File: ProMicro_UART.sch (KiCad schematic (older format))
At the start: 54 parts, among them J2 Conn_01x06, J3 USB_B_Mini, U1 FT232H, U2 93CxxB, U3 AZ1117-3.3, Y1 12Mhz

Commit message: renamed files
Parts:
- removed JP10, JP11: Jumper_NO_Small, Jumper:SolderJumper-2_P1.3mm_Open_RoundedPad1.0x1.5mm, symbol Device:Jumper_NO_Small
- added JP10, JP11: Jumper_3_Bridged12, Jumper:SolderJumper-3_P1.3mm_Open_RoundedPad1.0x1.5mm, symbol Jumper:Jumper_3_Bridged12
- added U4: FT232RL, Package_DFN_QFN:QFN-32-1EP_5x5mm_P0.5mm_EP3.1x3.1mm, symbol Interface_USB:FT232RL
- C14: value 100n -> 1µ
- LOGO1: footprint Symbol:OSHW-Logo_5.7x6mm_SilkScreen -> Symbol:OSHW-Symbol_6.7x6mm_SilkScreen
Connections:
- net ADBUS0: now also JP10.3 (B), JP11.1 (A)
- net ADBUS1: now also JP10.1 (A), JP11.3 (B)
- net D0: now also JP11.2 (C)
- net D1: now also JP10.2 (C)
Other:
- note added: "ATTENTION:\nRXD & TXD are swapped here!"
- note added: "RXD & TXD\ncan swapped here"
- note added: "VBAT/2"
- note removed: "VBAT"
- moved on the sheet: C13, C14, JP12, JP13, JP14, JP15, U3

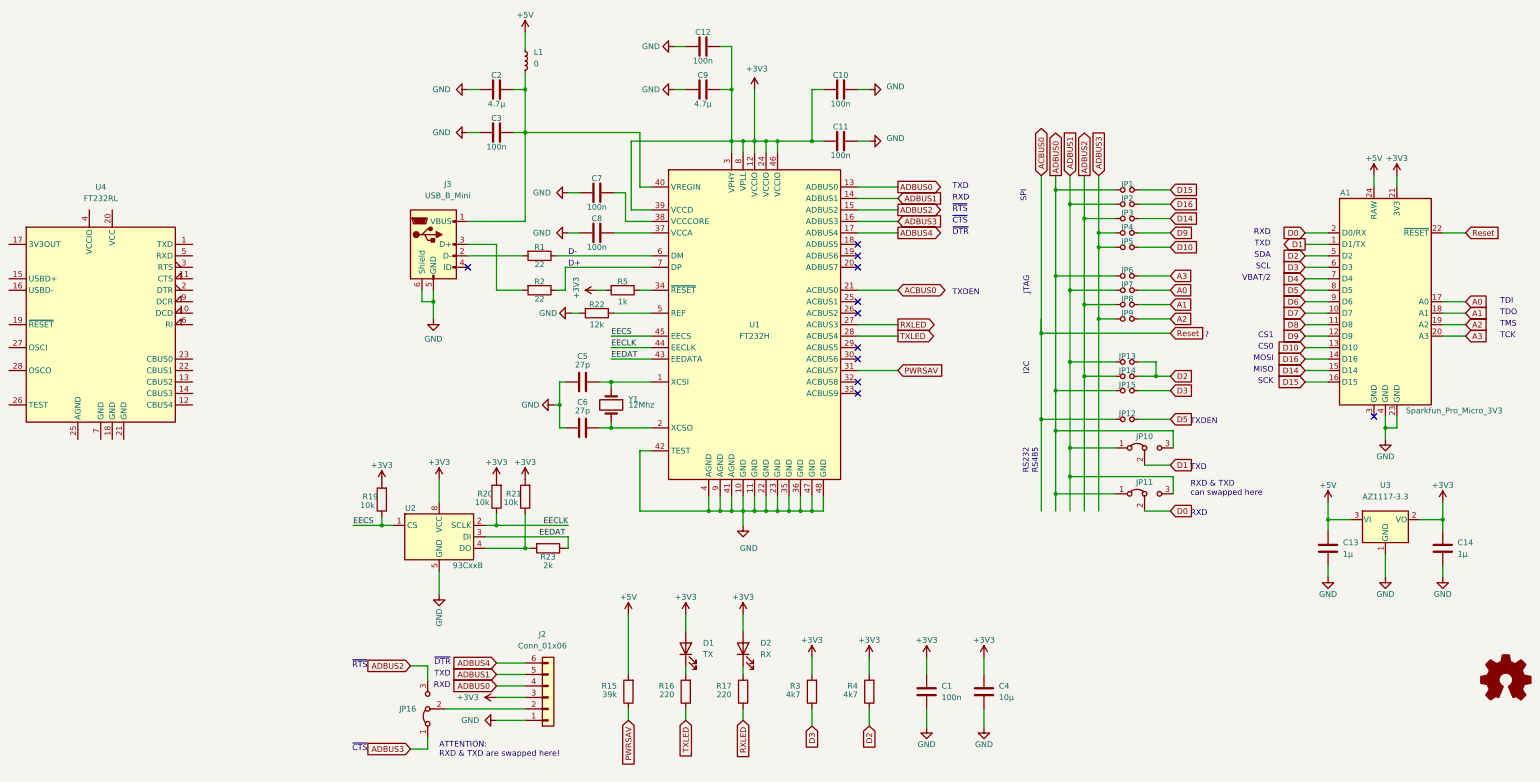
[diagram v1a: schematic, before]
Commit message: fully routed
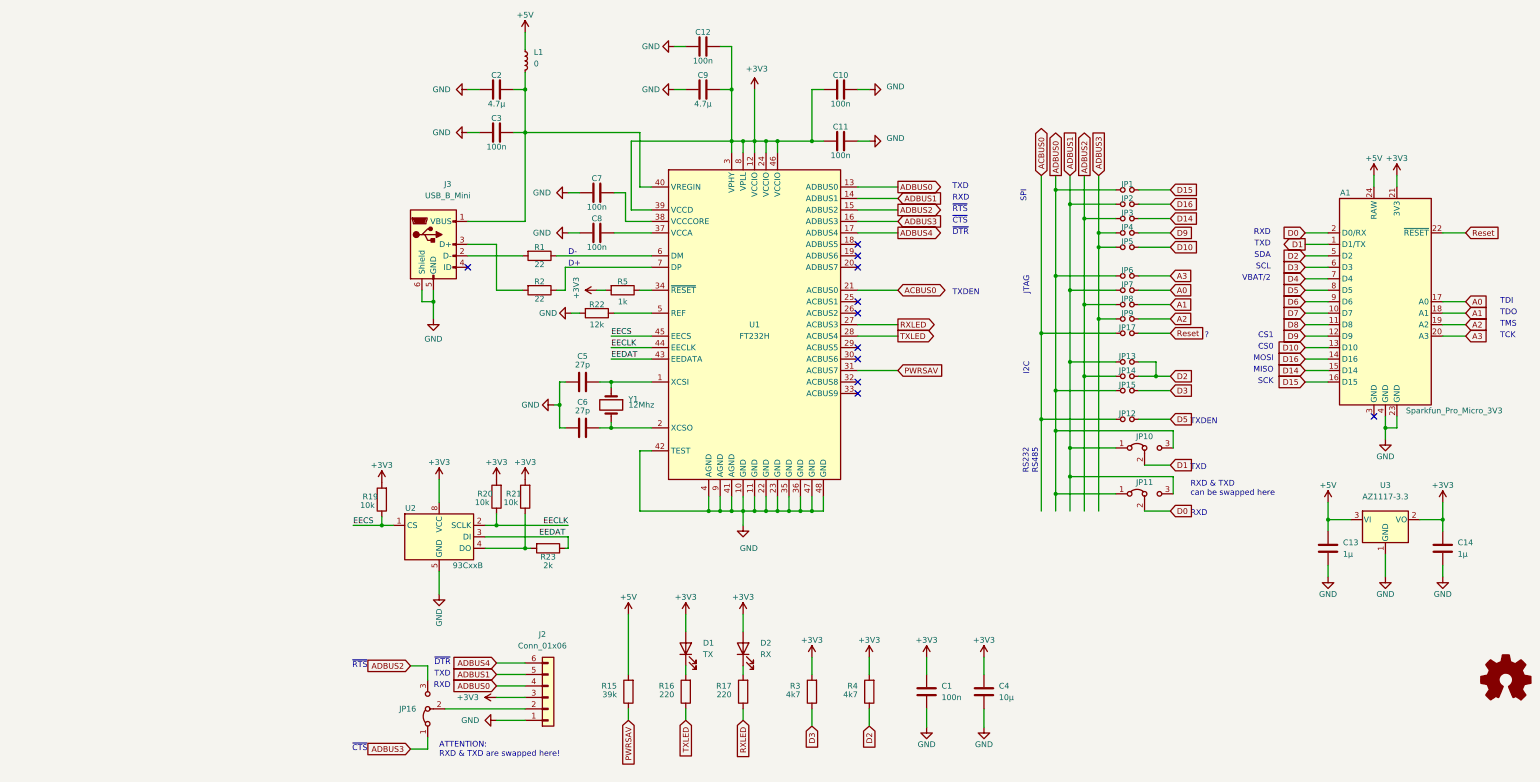
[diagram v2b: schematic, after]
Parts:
- removed U4: FT232RL, Package_DFN_QFN:QFN-32-1EP_5x5mm_P0.5mm_EP3.1x3.1mm, symbol Interface_USB:FT232RL
- added JP17: Jumper_NO_Small, Jumper:SolderJumper-2_P1.3mm_Open_RoundedPad1.0x1.5mm, symbol Device:Jumper_NO_Small
- U1: footprint Package_DFN_QFN:QFN-48-1EP_8x8mm_P0.5mm_EP6.2x6.2mm -> Package_QFP:LQFP-48_7x7mm_P0.5mm
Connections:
- net ACBUS0: now also JP17.1; no longer A1.22 (~RESET)
- new net Reset: A1.22 (~RESET), JP17.2
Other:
- note added: "RXD & TXD\ncan be swapped here"
- note removed: "RXD & TXD\ncan swapped here"

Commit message: new docs
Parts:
- added JP?: Jumper_NO_Small, symbol Device:Jumper_NO_Small
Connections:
- net +3V3: now also JP?.2
- net +5V: now also JP?.1
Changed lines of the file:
@@
 U 1 1 5EE683B5
 P 9750 5500
-F 0 "U3" H 9750 5800 50  0000 C CNN
-F 1 "AZ1117-3.3" H 9750 5700 50  0000 C CNN
+F 0 "U3" H 9750 5700 50  0000 C CNN
+F 1 "AZ1117-3.3" H 9750 5625 50  0000 C CNN
 F 2 "Package_TO_SOT_SMD:SOT-23-5" H 9750 5750 50  0001 C CIN
 F 3 "https://www.diodes.com/assets/Datasheets/AZ1117.pdf" H 9750 5500 50  0001 C CNN
@@
 L power:+5V #PWR0135
 U 1 1 5EE78093
-P 9250 5350
-F 0 "#PWR0135" H 9250 5200 50  0001 C CNN
-F 1 "+5V" H 9250 5500 50  0000 C CNN
-F 2 "" H 9250 5350 50  0001 C CNN
-F 3 "" H 9250 5350 50  0001 C CNN
-	1    9250 5350
+P 9250 5150
+F 0 "#PWR0135" H 9250 5000 50  0001 C CNN
+F 1 "+5V" H 9250 5300 50  0000 C CNN
+F 2 "" H 9250 5150 50  0001 C CNN
+F 3 "" H 9250 5150 50  0001 C CNN
+	1    9250 5150
 	1    0    0    -1
 $EndComp
@@
 L power:+3V3 #PWR0136
 U 1 1 5EE7895F
-P 10250 5350
-F 0 "#PWR0136" H 10250 5200 50  0001 C CNN
-F 1 "+3V3" H 10250 5500 50  0000 C CNN
-F 2 "" H 10250 5350 50  0001 C CNN
-F 3 "" H 10250 5350 50  0001 C CNN
-	1    10250 5350
+P 10250 5150
+F 0 "#PWR0136" H 10250 5000 50  0001 C CNN
+F 1 "+3V3" H 10250 5300 50  0000 C CNN
+F 2 "" H 10250 5150 50  0001 C CNN
+F 3 "" H 10250 5150 50  0001 C CNN
+	1    10250 5150
 	1    0    0    -1
 $EndComp
@@
 Connection ~ 9250 5500
 Wire Wire Line
-	9250 5500 9250 5350
+	9250 5500 9250 5175
 Wire Wire Line
 	10050 5500 10250 5500
 Wire Wire Line
-	10250 5500 10250 5350
+	10250 5500 10250 5175
 Wire Wire Line
 	10250 5600 10250 5500
@@
 Wire Wire Line
 	6750 3875 6750 4625
+$Comp
+L Device:Jumper_NO_Small JP?
+U 1 1 5E6685A0
+P 9750 5175
+F 0 "JP?" H 9750 5250 50  0000 C CNN
+F 1 "Jumper_NO_Small" H 9775 5275 50  0001 C CNN
+F 2 "" H 9750 5175 50  0001 C CNN
+F 3 "~" H 9750 5175 50  0001 C CNN
+	1    9750 5175
+	1    0    0    -1
+$EndComp
+Wire Wire Line
+	9850 5175 10250 5175
+Connection ~ 10250 5175
+Wire Wire Line
+	10250 5175 10250 5150
+Wire Wire Line
+	9650 5175 9250 5175
+Connection ~ 9250 5175
+Wire Wire Line
+	9250 5175 9250 5150
 $EndSCHEMATC
